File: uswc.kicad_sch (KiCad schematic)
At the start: 68 parts, among them J1 USB_C_Receptacle_USB2.0_16P, J2 debug-port, J3 USB_B_Micro, J4 jlink, P1 DFP, SW1 DUT prot sel, SW2 orient sel, SW3 DUT prot sel, U1 FE1.1s, U10 SRV05-4, U2 W25Q32JVZP, U3 AT24CS01-STUM, U4 RP2040, U5 XC6206PxxxMR, U6 TXB0102DCU, U7 LM397, U8 ADG884xRM, U9 SRV05-4, Y1 12MHz 10ppm, Y2 12MHz 10ppm

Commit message: fab jingtuo
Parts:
- added R18, R19: 4.7k, Resistor_SMD:R_0603_1608Metric, symbol Device:R
- added TP5: VBUS, TestPoint:TestPoint_THTPad_D1.5mm_Drill0.7mm, symbol Connector:TestPoint
- added TP6: GND, TestPoint:TestPoint_Bridge_Pitch2.0mm_Drill0.7mm, symbol Connector:TestPoint
- added TP7: 3V3, TestPoint:TestPoint_THTPad_D1.5mm_Drill0.7mm, symbol Connector:TestPoint
- FB1: footprint Inductor_SMD_Wurth:L_Wurth_WE-LQSH-2512 -> Inductor_SMD:L_0805_2012Metric; LCSC# (none) -> C1015
- J1: LCSC# (none) -> C165948
- J3: value USB_B_Micro -> USB3150-30-130-A
- P1: LCSC# (none) -> C5343530
- U8: LCSC# (none) -> C140435
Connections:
- net +3V3: now also TP7.1
- net GND: now also TP6.1; no longer J3.4 (ID)
- net HUB_3V3: now also R18.2, R19.2
- net VBUS: now also TP5.1
- net SCL: now reaches TP2.1, U1.23 (LED1/EESCL), U3.1 (SCL)
- net SCL: now also R18.1
- net SDA: now reaches TP1.1, U1.27 (TESTJ/EESDA), U3.3 (SDA)
- net SDA: now also R19.1
- no-connect marks 10 -> 11
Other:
- moved on the sheet: R6, TP1, TP2, TP3, U3

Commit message: fab 8012
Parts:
- P1: footprint lib:jingtuojin_918-118A2021S40000 -> lib:GT-USB-8012A; LCSC# C5343530 -> C2982483
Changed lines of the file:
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@@
 			)
 		)
-		(property "Footprint" "lib:jingtuojin_918-118A2021S40000"
+		(property "Footprint" "lib:GT-USB-8012A"
 			(at 38.1 114.3 0)
 			(effects
@@
 			)
 		)
-		(property "LCSC#" "C5343530"
+		(property "LCSC#" "C2982483"
 			(at 34.29 114.3 0)
 			(effects

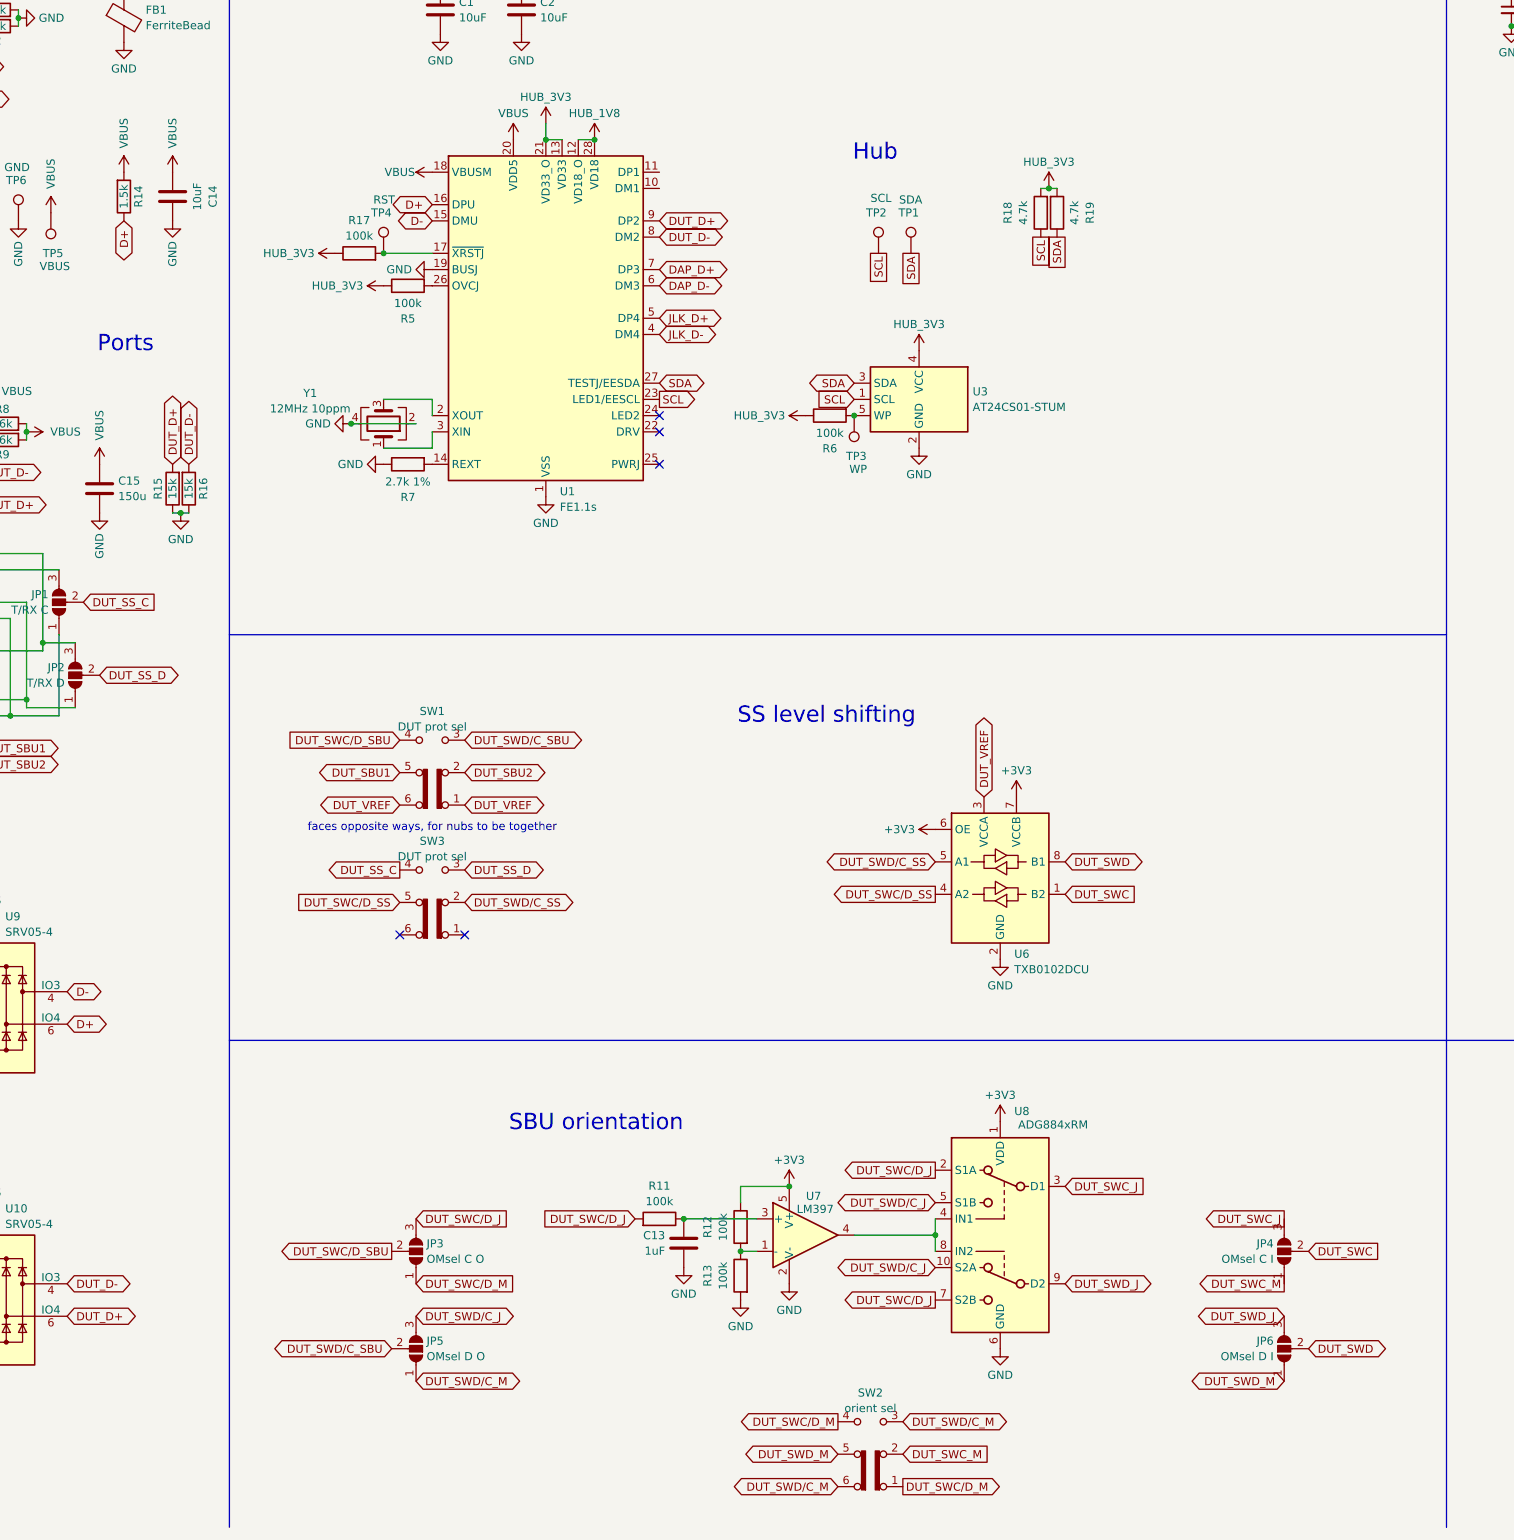
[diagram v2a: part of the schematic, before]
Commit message: 2 layer, analog switches
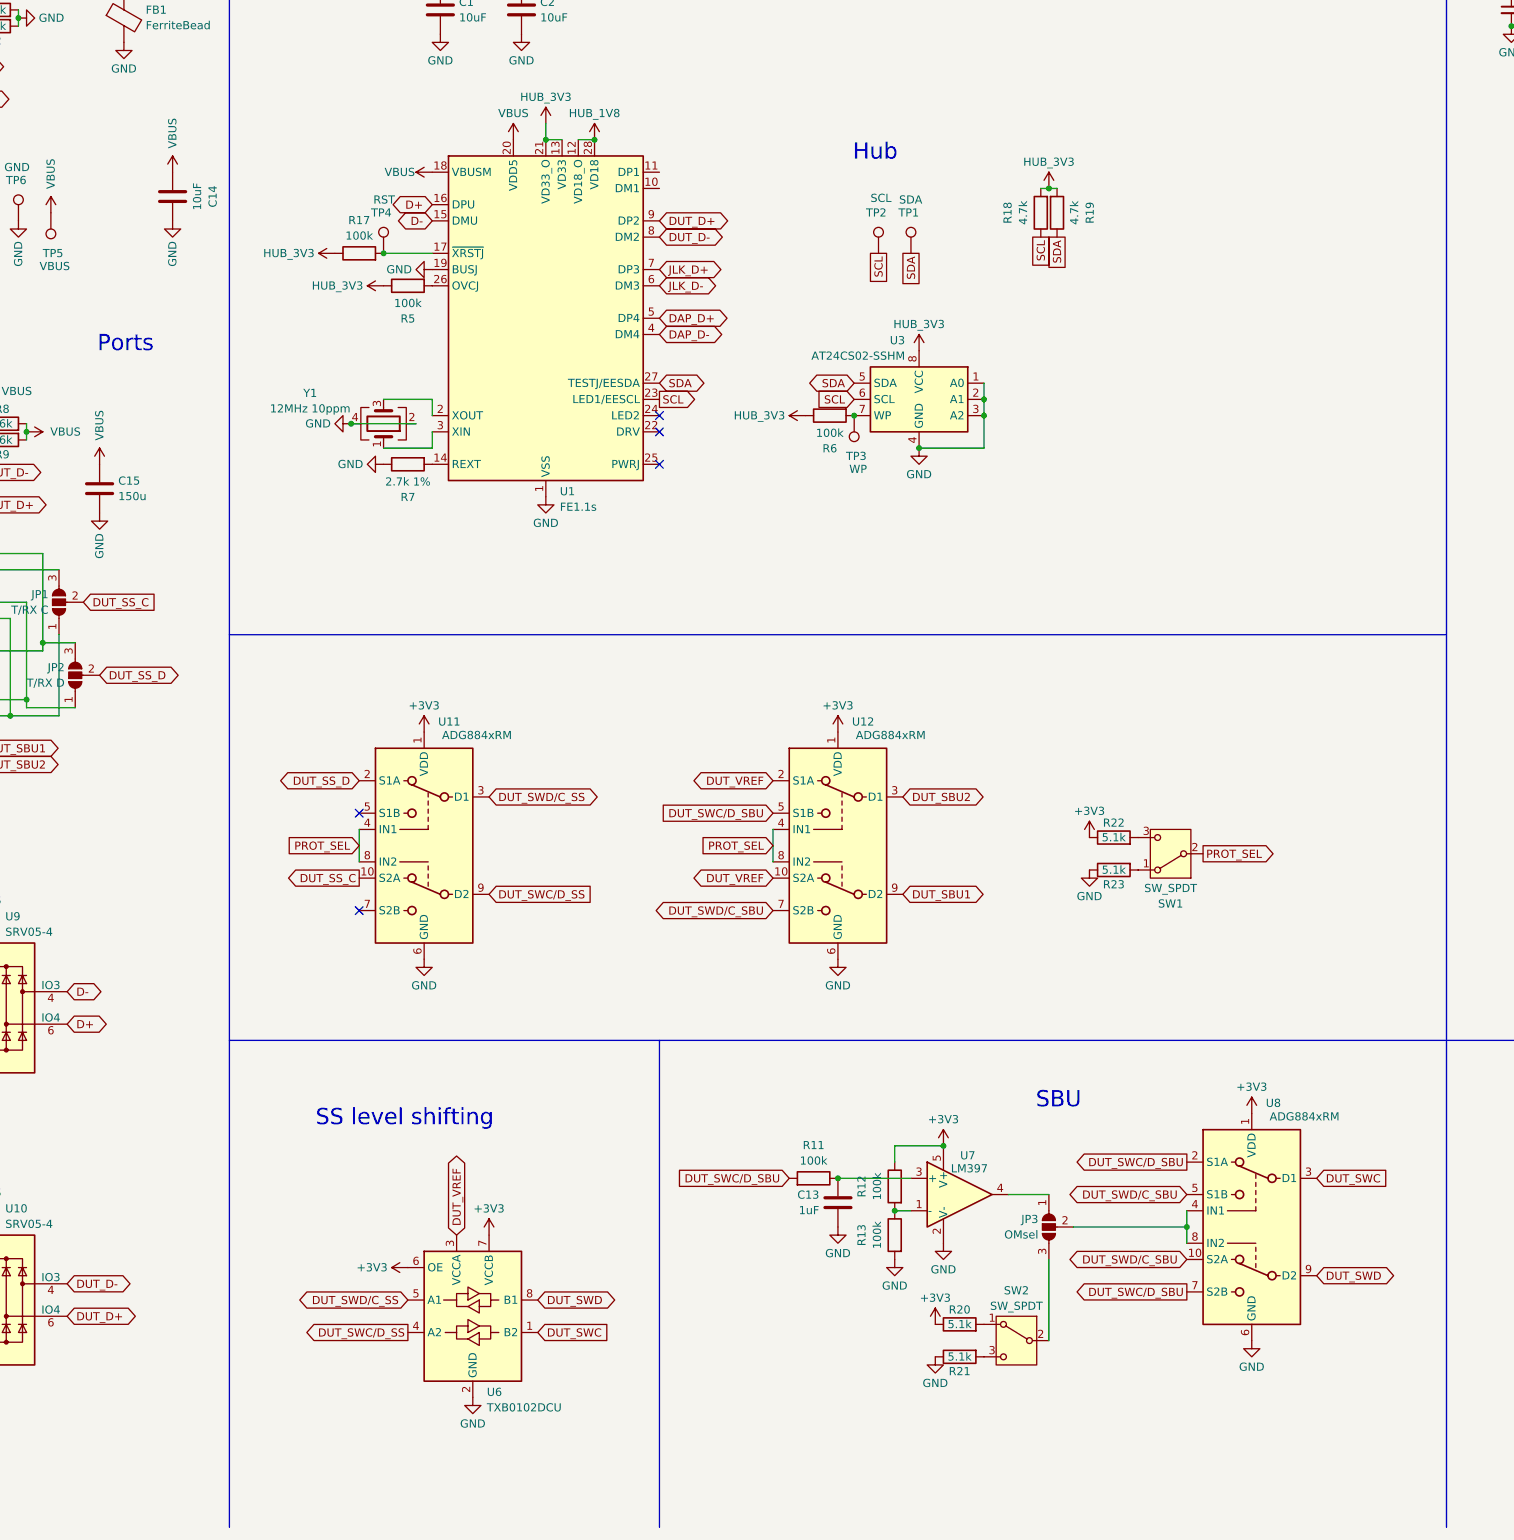
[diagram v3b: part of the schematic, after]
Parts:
- removed JP4: OMsel C I, Jumper:SolderJumper-3_P1.3mm_Open_RoundedPad1.0x1.5mm, symbol Jumper:SolderJumper_3_Open
- removed JP5: OMsel D O, Jumper:SolderJumper-3_P1.3mm_Open_RoundedPad1.0x1.5mm, symbol Jumper:SolderJumper_3_Open
- removed JP6: OMsel D I, Jumper:SolderJumper-3_P1.3mm_Open_RoundedPad1.0x1.5mm, symbol Jumper:SolderJumper_3_Open
- removed R14: 1.5k, Resistor_SMD:R_0603_1608Metric, symbol Device:R
- removed R15, R16: 15k, Resistor_SMD:R_0603_1608Metric, symbol Device:R
- removed SW1, SW3: DUT prot sel, lib:K3-1390S-D1, symbol Switch:SW_Slide_DPDT
- removed SW2: orient sel, lib:K3-1390S-D1, symbol Switch:SW_Slide_DPDT
- removed U3: AT24CS01-STUM, Package_TO_SOT_SMD:SOT-23-5, symbol Memory_EEPROM:AT24CS01-STUM
- added R20, R21, R22, R23: 5.1k, Resistor_SMD:R_0603_1608Metric, symbol Device:R
- added SW1, SW2: SW_SPDT, Button_Switch_SMD:SW_SPDT_PCM12, symbol Switch:SW_SPDT
- added U11, U12: ADG884xRM, Package_SO:MSOP-10_3x3mm_P0.5mm, symbol Analog_Switch:ADG884xRM
- added U3: AT24CS02-SSHM, Package_SO:SOIC-8_3.9x4.9mm_P1.27mm, symbol Memory_EEPROM:AT24CS02-SSHM
- J3, TP1, TP2, TP3, TP4, TP5, TP6, TP7, U7: now left out of the parts list
- JP3: value OMsel C O -> OMsel
- U1: LCSC# (none) -> C9359
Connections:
- net DUT_SWC_J is gone; now on net DUT_SWC: U8.3 (D1)
- net DUT_SWD_J is gone; now on net DUT_SWD: U8.9 (D2)
- net DUT_SWD/C_J is gone; now on net DUT_SWD/C_SBU: U8.10 (S2A), U8.5 (S1B)
- net +3V3: now also R20.1, R22.1, U11.1 (VDD), U12.1 (VDD)
- net DAP_D+: now also U1.5 (DP4); no longer U1.7 (DP3)
- net DAP_D-: now also U1.4 (DM4); no longer U1.6 (DM3)
- net DUT_SBU1: now also U12.9 (D2)
- net DUT_SBU2: now also U12.3 (D1)
- net DUT_SS_C: now also U11.10 (S2A)
- net DUT_SS_D: now also U11.2 (S1A)
- net DUT_SWC/D_SBU: now also R11.2, U8.2 (S1A), U8.7 (S2B), U12.5 (S1B); no longer JP3.2 (C)
- net DUT_SWC/D_SS: now also U11.9 (D2)
- net DUT_SWD/C_SBU: now also U12.7 (S2B)
- net DUT_SWD/C_SS: now also U11.3 (D1)
- net DUT_VREF: now also U12.10 (S2A), U12.2 (S1A)
- net GND: now also R21.1, R23.1, U11.6 (GND), U12.6 (GND), U3.1 (A0), U3.2 (A1), U3.3 (A2), U3.4 (GND)
- net HUB_3V3: now also U3.8 (VCC)
- net JLK_D+: now also U1.7 (DP3); no longer U1.5 (DP4)
- net JLK_D-: now also U1.6 (DM3); no longer U1.4 (DM4)
- net SCL: now also U3.6 (SCL)
- net SDA: now also U3.5 (SDA)
- net at U8.4 (IN1), U8.8 (IN2): now also JP3.2 (C); no longer U7.4
- net at R6.2, TP3.1: now also U3.7 (WP)
- removed net DUT_SWC/D_J: JP3.3 (B), R11.2, U8.2 (S1A), U8.7 (S2B)
- net DUT_SWC/D_M: no longer names the net of JP3.1 (A)
- net DUT_SWC/D_M: now also U7.4
- new net: JP3.3 (B), SW2.2 (B)
- new net: R21.2, SW2.3 (C)
- new net: R20.2, SW2.1 (A)
- new net: R23.2, SW1.1 (A)
- new net: R22.2, SW1.3 (C)
- new net PROT_SEL: SW1.2 (B), U11.4 (IN1), U11.8 (IN2), U12.4 (IN1), U12.8 (IN2)
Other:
- note added: "SBU"
- note removed: "SBU orientation"
- note removed: "faces opposite ways, for nubs to be together"
- moved on the sheet: C13, JP3, R11, R12, R13, U6, U7, U8

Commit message: pre level shifter
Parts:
- removed C13: 1uF, Capacitor_SMD:C_0603_1608Metric, symbol Device:C
- removed C2: 10uF, Capacitor_SMD:C_0603_1608Metric, symbol Device:C
- removed J1: USB_C_Receptacle_USB2.0_16P, Connector_USB:USB_C_Receptacle_HRO_TYPE-C-31-M-12, symbol Connector:USB_C_Receptacle_USB2.0_16P
- removed JP1: T/RX C, Jumper:SolderJumper-3_P1.3mm_Open_RoundedPad1.0x1.5mm, symbol Jumper:SolderJumper_3_Open
- removed JP2: T/RX D, Jumper:SolderJumper-3_P1.3mm_Open_RoundedPad1.0x1.5mm, symbol Jumper:SolderJumper_3_Open
- removed JP3: OMsel, Jumper:SolderJumper-3_P1.3mm_Open_RoundedPad1.0x1.5mm, symbol Jumper:SolderJumper_3_Open
- removed R11, R12, R13, R17, R5, R6: 100k, Resistor_SMD:R_0603_1608Metric, symbol Device:R
- removed R18, R19: 4.7k, Resistor_SMD:R_0603_1608Metric, symbol Device:R
- removed R20, R21: 5.1k, Resistor_SMD:R_0603_1608Metric, symbol Device:R
- removed R7: 2.7k 1%, Resistor_SMD:R_0603_1608Metric, symbol Device:R
- removed SW2: SW_SPDT, Button_Switch_SMD:SW_SPDT_PCM12, symbol Switch:SW_SPDT
- removed TP1: SDA, TestPoint:TestPoint_THTPad_D1.5mm_Drill0.7mm, symbol Connector:TestPoint
- removed TP2: SCL, TestPoint:TestPoint_THTPad_D1.5mm_Drill0.7mm, symbol Connector:TestPoint
- removed TP3: WP, TestPoint:TestPoint_THTPad_D1.5mm_Drill0.7mm, symbol Connector:TestPoint
- removed TP4: RST, TestPoint:TestPoint_THTPad_D1.5mm_Drill0.7mm, symbol Connector:TestPoint
- removed U11, U12, U8: ADG884xRM, Package_SO:MSOP-10_3x3mm_P0.5mm, symbol Analog_Switch:ADG884xRM
- removed U3: AT24CS02-SSHM, Package_SO:SOIC-8_3.9x4.9mm_P1.27mm, symbol Memory_EEPROM:AT24CS02-SSHM
- removed U6: TXB0102DCU, Package_SO:VSSOP-8_2.3x2mm_P0.5mm, symbol Logic_LevelTranslator:TXB0102DCU
- added D1: LED, LED_SMD:LED_0805_2012Metric, symbol Device:LED
- added J1: USB_C_Receptacle, Connector_USB:USB_C_Receptacle_Amphenol_12401548E4-2A, symbol Connector:USB_C_Receptacle
- added R14, R16: 56k, Resistor_SMD:R_0603_1608Metric, symbol Device:R
- added R15: 1k, Resistor_SMD:R_0603_1608Metric, symbol Device:R
- added SW3: SW_SPDT, Button_Switch_SMD:SW_SPDT_PCM12, symbol Switch:SW_SPDT
- added SW4: SW_Push, Button_Switch_SMD:SW_SPST_B3U-1000P, symbol Switch:SW_Push
- added TP1, TP10, TP11, TP2, TP3, TP4, TP8, TP9: inline, TestPoint:TestPoint_Pad_D1.0mm, symbol Connector:TestPoint_Small
- added U11, U14, U17: ~, Package_DFN_QFN:UQFN-16_1.8x2.6mm_P0.4mm, symbol misc:FSA2567UMX
- added U3: 74LVC1G3157, Package_TO_SOT_SMD:SOT-363_SC-70-6, symbol 74xGxx:74LVC1G3157
- added U6: TXB0104RUT, Package_DFN_QFN:Texas_R-PUQFN-N12, symbol Logic_LevelTranslator:TXB0104RUT
- C1: value 10uF -> 1uF
- P1: footprint lib:GT-USB-8012A -> lib:jingtuojin_918-118A2021Y40005; LCSC# C2982483 -> C2763098
- R10: value 100k -> 56k
- U1: value FE1.1s -> ~; footprint Package_SO:SSOP-28_3.9x9.9mm_P0.635mm -> Package_SO:QSOP-16_3.9x4.9mm_P0.635mm; symbol Interface_USB:FE1.1s -> Interface_USB:CH334R; LCSC# C9359 -> C4154405
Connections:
- net +3V3: now also R14.2, R15.2, R16.2, U11.14 (VDD), U14.14 (VDD), U17.14 (VDD), U3.5 (VCC), U6.11 (VCCB)
- net D+: now also U1.11 (DPU+), J1.A6 (D+), J1.B6 (D+); no longer U1.16 (DPU)
- net D-: now also U1.10 (DMU-), J1.A7 (D-), J1.B7 (D-); no longer U1.15 (DMU)
- net DAP_D+: now also U1.2 (DP4+); no longer U1.5 (DP4)
- net DAP_D-: now also U1.1 (DM4-); no longer U1.4 (DM4)
- net DUT_D+: now also U1.4 (DP3+); no longer U1.9 (DP2)
- net DUT_D-: now also U1.3 (DM3-); no longer U1.8 (DM2)
- net DUT_SWC/D_SBU: now also U14.1 (S1A), U14.13 (S4A), U14.7 (S3B)
- net DUT_SWD/C_SBU: now also U14.11 (S4B), U14.5 (S2A), U14.9 (S3A)
- net DUT_VREF: now also U3.4, U6.1 (VCCA)
- net GND: now also C1.1, U1.14 (GND), J1.A1 (GND), J1.A12 (GND), J1.B1 (GND), J1.B12 (GND), SW4.1, U11.6 (GND), U14.6 (GND), U17.6 (GND), U3.2 (GND), U6.6 (GND); no longer C1.2, U1.1 (VSS), U1.19 (BUSJ)
- net JLK_D+: now also U1.8 (DP1+); no longer U1.7 (DP3)
- net JLK_D-: now also U1.7 (DM1-); no longer U1.6 (DM3)
- net SHIELD: now also J1.S1 (SHIELD)
- net VBUS: now also U1.12 (V5), J1.A4 (VBUS), J1.A9 (VBUS), J1.B4 (VBUS), J1.B9 (VBUS); no longer U1.18 (VBUSM), U1.20 (VDD5)
- net SS_DIR: now reaches U7.4
- net SS_DIR: now also R16.1, U17.2 (SEL), U3.6
- net DUT_VREF_A: now reaches U7.1 (-)
- net DUT_VREF_A: now also U14.3 (S2B), U3.1
- net DUT_VREF_B: now reaches U7.3 (+)
- net DUT_VREF_B: now also U14.15 (S1B), U3.3
- net at P1.A3 (TX1-): no longer P1.B3 (TX2-)
- net SS_A10: now reaches P1.A10 (RX2-)
- net SS_A10: now also U17.1 (S1A), U17.7 (S3B); no longer P1.B10 (RX1-)
- net BOOT: now reaches U2.1 (~{CS}), U4.56 (QSPI_SS)
- net BOOT: now also R14.1, SW4.2
- net at R23.2, SW1.1 (A): now also SW3.1 (A)
- net at R22.2, SW1.3 (C): now also SW3.3 (C)
- net at Y1.3: now also U1.15 (XO); no longer U1.2 (XOUT)
- net at Y1.1: now also U1.16 (XI); no longer U1.3 (XIN)
- net at P1.A2 (TX1+): no longer P1.B2 (TX2+)
- net SS_A11: now reaches P1.A11 (RX2+)
- net SS_A11: now also U17.13 (S4A), U17.5 (S2A); no longer P1.B11 (RX1+)
- net at R1.1: now also J1.A5 (CC1)
- net at R2.1: now also J1.B5 (CC2)
- net DUT_SWO/TDO_J: now reaches J4.6 (SWO)
- net DUT_SWO/TDO_J: now also U11.9 (S3A)
- net DUT_TDI_J: now reaches J4.8 (TDI)
- net DUT_TDI_J: now also U11.13 (S4A)
- net DUT_TDI_P: now reaches U4.18 (GPIO15)
- net DUT_TDI_P: now also U11.11 (S4B)
- net at U4.29 (GPIO18): now also D1.1 (K)
- net DUT_SBU1 renamed DUT_SBU_A
- net DUT_SBU_A: now also U14.4 (D2)
- net DUT_SBU2 renamed DUT_SBU_B
- net DUT_SBU_B: now also U14.16 (D1)
- net DUT_SWC renamed DUT_SWC/TCK_J
- net DUT_SWC/TCK_J: now also U11.5 (S2A); no longer U4.15 (GPIO12)
- net DUT_SWD renamed DUT_SWD/TMS_J
- net DUT_SWD/TMS_J: now also U11.1 (S1A); no longer U4.16 (GPIO13)
- net DUT_SWD_IN renamed DUT_SWO/TDO_P
- net DUT_SWO/TDO_P: now also U11.7 (S3B)
- removed net HUB_1V8: U1.12 (VD18_O), U1.28 (VD18)
- removed net HUB_3V3: C1.1, U1.13 (VD33), U1.21 (VD33_O)
- net PROT_SEL renamed USE_SS
- net USE_SS: now also U14.2 (SEL), U6.12 (OE)
- removed net SCL: U1.23 (LED1/EESCL)
- removed net SDA: U1.27 (TESTJ/EESDA)
- new net: D1.2 (A), R15.1
- new net: C1.2, U1.13 (VDD33)
- new net DUT_SWC/TCK: TP2.1, U11.4 (D2), U14.8 (D3), U6.9 (B2)
- new net DUT_SWC/TCK_P: U11.3 (S2B), U4.15 (GPIO12)
- new net DUT_SWD/TMS: TP1.1, U11.16 (D1), U14.12 (D4), U6.10 (B1)
- new net DUT_SWD/TMS_P: U11.15 (S1B), U4.16 (GPIO13)
- new net DUT_SWO/TDO: TP3.1, U11.8 (D3), U6.8 (B3)
- new net DUT_TDI: TP4.1, U11.12 (D4), U6.7 (B4)
- new net SS_A10_NORM: TP9.1, U17.8 (D3), U6.4 (A3)
- new net SS_A11_NORM: TP8.1, U17.12 (D4), U6.5 (A4)
- new net SS_B10: P1.B10 (RX1-), U17.15 (S1B), U17.9 (S3A)
- new net SS_B10_NORM: TP11.1, U17.16 (D1), U6.2 (A1)
- new net SS_B11: P1.B11 (RX1+), U17.11 (S4B), U17.3 (S2B)
- new net SS_B11_NORM: TP10.1, U17.4 (D2), U6.3 (A2)
- new net USE_PICO: SW3.2 (B), U11.2 (SEL)
- no-connect marks 11 -> 8
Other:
- moved on the sheet: C1, C14, C15, FB1, P1, R1, R2, R22, R23, R8, R9, SW1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

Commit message: pre only pico
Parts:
- removed R16: 56k, Resistor_SMD:R_0603_1608Metric, symbol Device:R
- removed TP1, TP10, TP11, TP2, TP3, TP4, TP8, TP9: inline, TestPoint:TestPoint_Pad_D1.0mm, symbol Connector:TestPoint_Small
- removed U17: ~, Package_DFN_QFN:UQFN-16_1.8x2.6mm_P0.4mm, symbol misc:FSA2567UMX
- removed U3: 74LVC1G3157, Package_TO_SOT_SMD:SOT-363_SC-70-6, symbol 74xGxx:74LVC1G3157
- removed U6: TXB0104RUT, Package_DFN_QFN:Texas_R-PUQFN-N12, symbol Logic_LevelTranslator:TXB0104RUT
- removed U7: LM397, Package_TO_SOT_SMD:SOT-23-5, symbol Comparator:LM397
- added U3: SN74LVC1T45DBV, Package_TO_SOT_SMD:SOT-23-6, symbol Logic_LevelTranslator:SN74LVC1T45DBV
- added U6: 74LVC1G125, symbol 74xGxx:74LVC1G125
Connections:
- net SS_B10 is gone; now on net SS_AB10: P1.B10 (RX1-)
- net SS_B11 is gone; now on net SS_AB11: P1.B11 (RX1+)
- net +3V3: now also U3.6 (VCCB)
- net DUT_SWC/D_SBU: no longer U14.13 (S4A), U14.7 (S3B)
- net DUT_SWD/C_SBU: no longer U14.11 (S4B), U14.9 (S3A)
- net DUT_SWO/TDO_J: no longer U11.9 (S3A)
- net DUT_TDI_J: no longer U11.13 (S4A)
- net DUT_VREF: now also U3.1 (VCCA), U6.5 (VCC)
- net GND: now also U3.2 (GND), U6.1, U6.3 (GND)
- net DUT_SWDIR_P: now reaches U4.14 (GPIO11)
- net DUT_SWDIR_P: now also U3.5 (DIR)
- net DUT_SWC/TCK renamed DUT_SWC
- net DUT_SWC: now also U14.11 (S4B); no longer U14.8 (D3)
- net DUT_SWC/TCK_J renamed DUT_SWC_J
- net DUT_SWC/TCK_P renamed DUT_SWC_P
- net DUT_SWC_P: now also U6.2; no longer U11.3 (S2B)
- net DUT_SWD/TMS renamed DUT_SWD
- net DUT_SWD: now also U14.7 (S3B); no longer U14.12 (D4)
- net DUT_SWD/TMS_J renamed DUT_SWD_J
- net DUT_SWD/TMS_P renamed DUT_SWD_P
- net DUT_SWD_P: now also U3.4 (B); no longer U11.15 (S1B)
- net DUT_SWO/TDO: no longer names the net of U11.8 (D3)
- net DUT_SWO/TDO_P: no longer names the net of U11.7 (S3B)
- net DUT_SWO/TDO_P: no longer U4.17 (GPIO14)
- net DUT_TDI: no longer names the net of U11.12 (D4)
- net DUT_TDI_P: no longer names the net of U11.11 (S4B)
- net DUT_TDI_P: no longer U4.18 (GPIO15)
- net SS_A10 renamed SS_AB10
- net SS_AB10: now also U14.8 (D3)
- net SS_A11 renamed SS_AB11
- net SS_AB11: now also U14.12 (D4)
- new net DUT_SWC_P_L: U11.3 (S2B), U6.4
- new net DUT_SWD_P_L: U11.15 (S1B), U3.3 (A)
- no-connect marks 8 -> 10
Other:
- moved on the sheet: U11
